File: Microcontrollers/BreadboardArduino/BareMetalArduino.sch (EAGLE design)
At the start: 8 parts, among them IC1 ATMEGA168-20P, SW1 SPST_TACT-EVQQ2

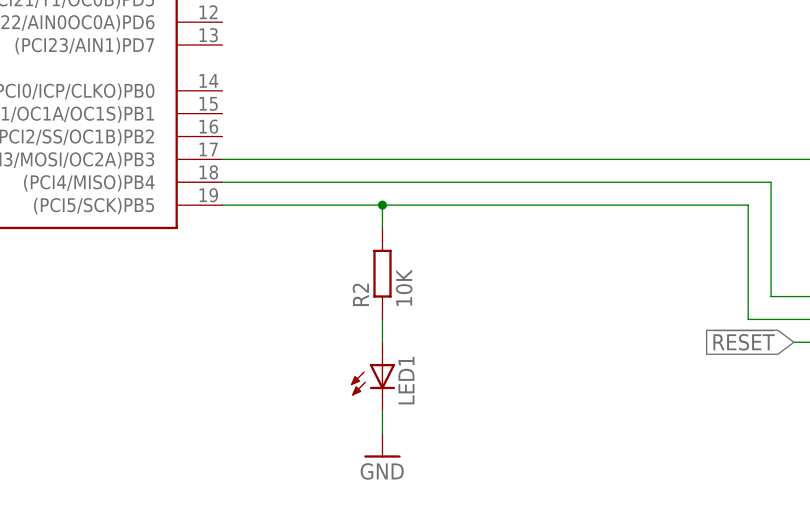
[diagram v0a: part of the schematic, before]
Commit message: Changed LED series resistor to a sane value
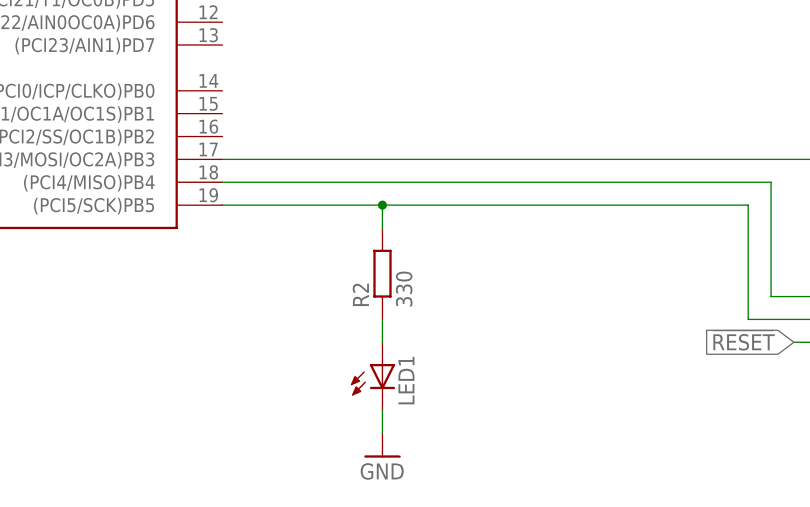
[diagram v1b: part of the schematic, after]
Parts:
- R2: value 10K -> 330
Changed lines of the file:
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@@
 <part name="P+3" library="supply1" deviceset="+5V" device=""/>
 <part name="LED1" library="led" deviceset="LED" device="5MM"/>
-<part name="R2" library="rcl" deviceset="R-EU_" device="0207/15" value="10K"/>
+<part name="R2" library="rcl" deviceset="R-EU_" device="0207/15" value="330"/>
 <part name="GND4" library="supply1" deviceset="GND" device=""/>
 <part name="SW1" library="adafruit" deviceset="SPST_TACT" device="-EVQQ2"/>

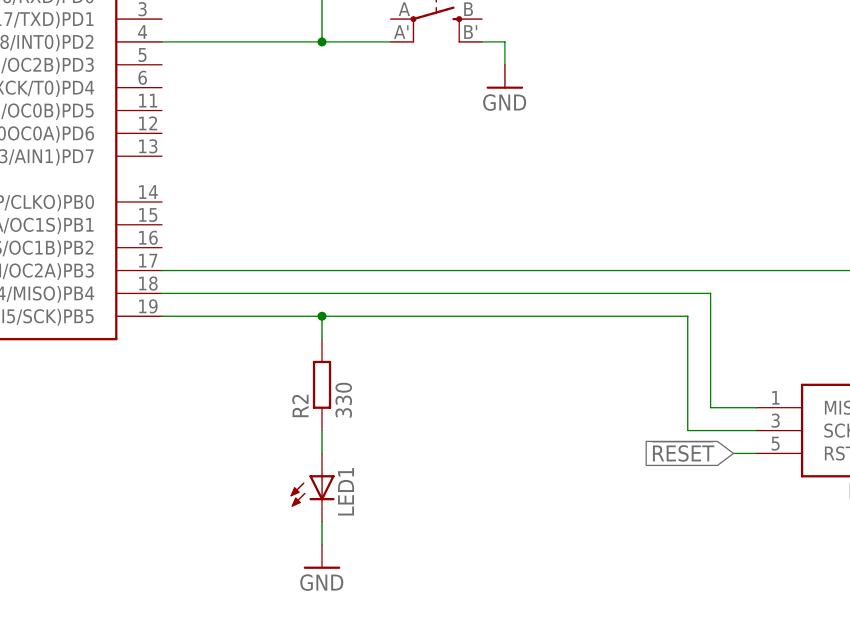
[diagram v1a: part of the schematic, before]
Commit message: Moved LED to PB0
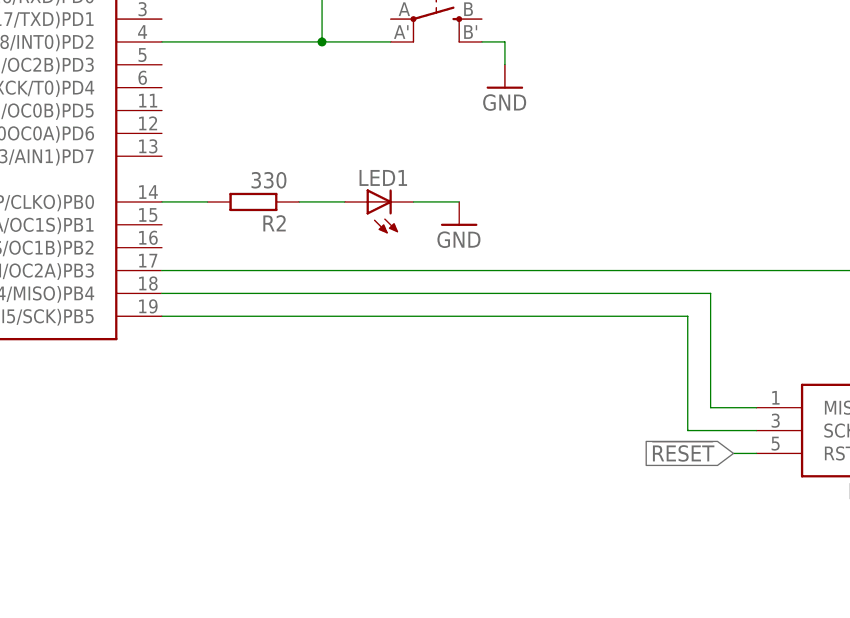
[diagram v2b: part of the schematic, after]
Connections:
- new net N$1: IC1.(PCI0/ICP/CLKO)PB0, R2.2
- net N$5: no longer R2.2
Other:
- moved on the sheet: LED1, R2
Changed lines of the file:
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@@
 <instance part="GND3" gate="1" x="226.06" y="53.34"/>
 <instance part="P+3" gate="1" x="226.06" y="73.66"/>
-<instance part="LED1" gate="G$1" x="147.32" y="55.88"/>
-<instance part="R2" gate="G$1" x="147.32" y="66.04" rot="R90"/>
-<instance part="GND4" gate="1" x="147.32" y="45.72"/>
+<instance part="LED1" gate="G$1" x="152.4" y="86.36" rot="R90"/>
+<instance part="R2" gate="G$1" x="139.7" y="86.36" rot="R180"/>
+<instance part="GND4" gate="1" x="162.56" y="83.82"/>
 <instance part="SW1" gate="G$1" x="160.02" y="106.68" rot="R270"/>
 <instance part="GND5" gate="1" x="167.64" y="99.06"/>
@@
 <segment>
 <pinref part="LED1" gate="G$1" pin="C"/>
-<wire x1="147.32" y1="50.8" x2="147.32" y2="48.26" width="0.1524" layer="91"/>
+<wire x1="157.48" y1="86.36" x2="162.56" y2="86.36" width="0.1524" layer="91"/>
 <pinref part="GND4" gate="1" pin="GND"/>
 </segment>
@@
 <wire x1="187.96" y1="60.96" x2="187.96" y2="73.66" width="0.1524" layer="91"/>
 <pinref part="IC1" gate="G$1" pin="(PCI5/SCK)PB5"/>
-<wire x1="187.96" y1="73.66" x2="147.32" y2="73.66" width="0.1524" layer="91"/>
-<pinref part="R2" gate="G$1" pin="2"/>
-<wire x1="147.32" y1="73.66" x2="129.54" y2="73.66" width="0.1524" layer="91"/>
-<wire x1="147.32" y1="71.12" x2="147.32" y2="73.66" width="0.1524" layer="91"/>
-<junction x="147.32" y="73.66"/>
+<wire x1="187.96" y1="73.66" x2="129.54" y2="73.66" width="0.1524" layer="91"/>
 </segment>
 </net>
@@
 <pinref part="R2" gate="G$1" pin="1"/>
 <pinref part="LED1" gate="G$1" pin="A"/>
-<wire x1="147.32" y1="60.96" x2="147.32" y2="58.42" width="0.1524" layer="91"/>
+<wire x1="144.78" y1="86.36" x2="149.86" y2="86.36" width="0.1524" layer="91"/>
 </segment>
 </net>
@@
 </segment>
 </net>
+<net name="N$1" class="0">
+<segment>
+<pinref part="R2" gate="G$1" pin="2"/>
+<pinref part="IC1" gate="G$1" pin="(PCI0/ICP/CLKO)PB0"/>
+<wire x1="134.62" y1="86.36" x2="129.54" y2="86.36" width="0.1524" layer="91"/>
+</segment>
+</net>
